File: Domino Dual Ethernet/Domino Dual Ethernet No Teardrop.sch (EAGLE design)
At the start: 38 parts, among them J1 B59(57-02)F4-03-1212-C12, J2 MH18-1, J3 MH18-1

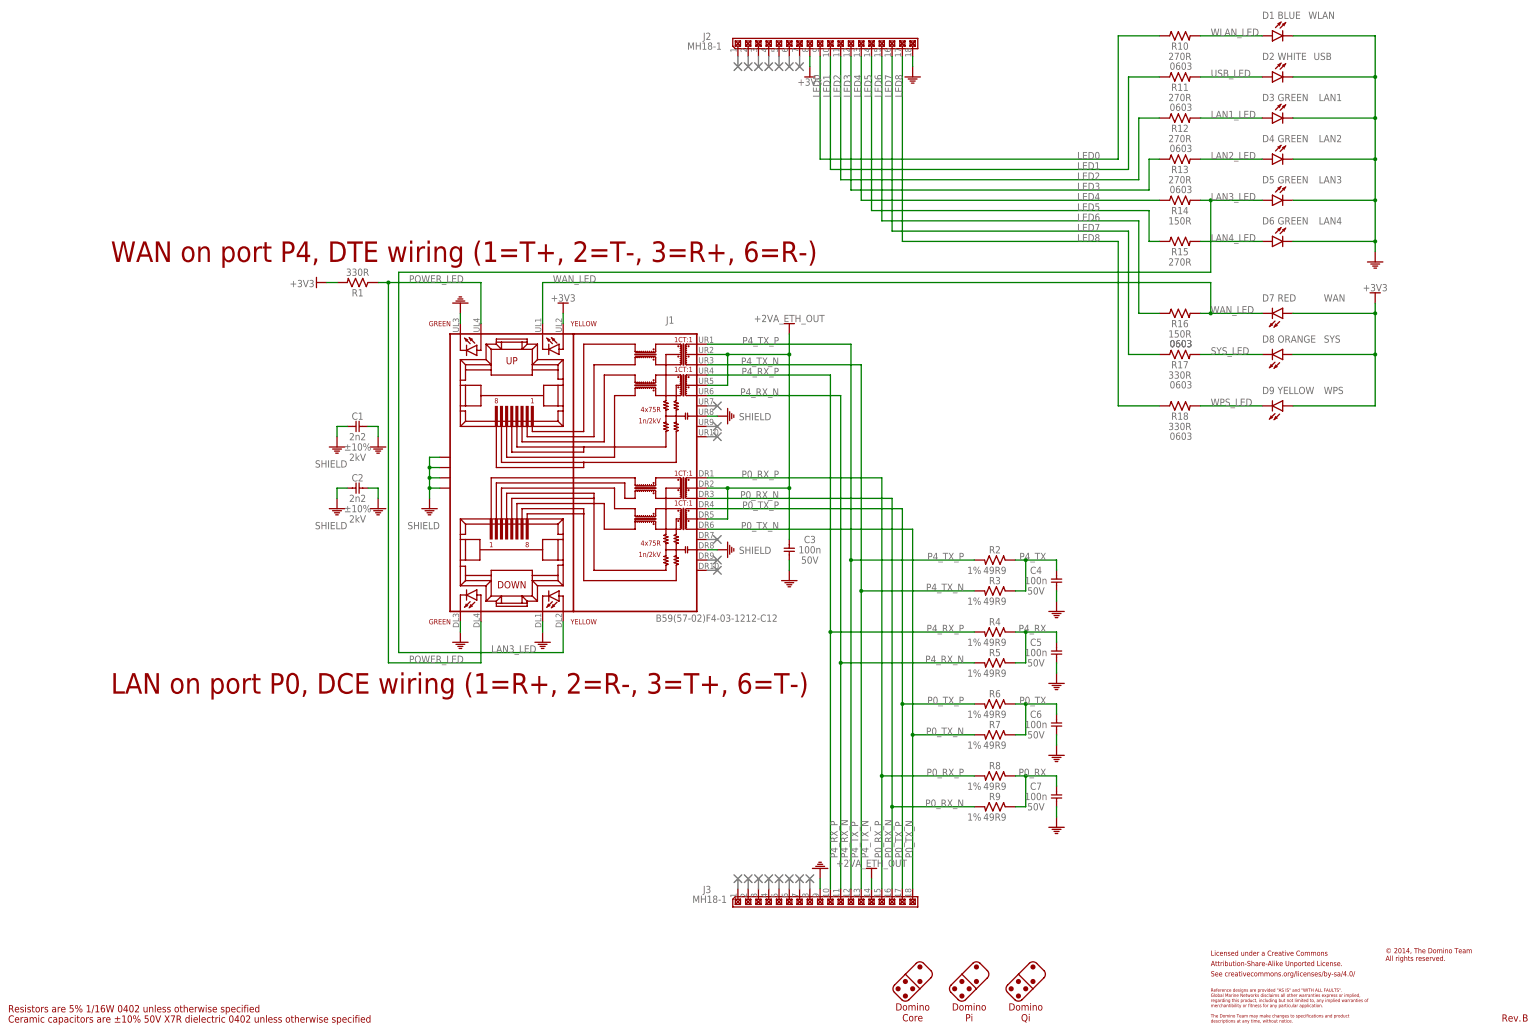
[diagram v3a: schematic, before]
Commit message: Replaced RJ45 Jack with one model without LED in Dual Ethernet tile
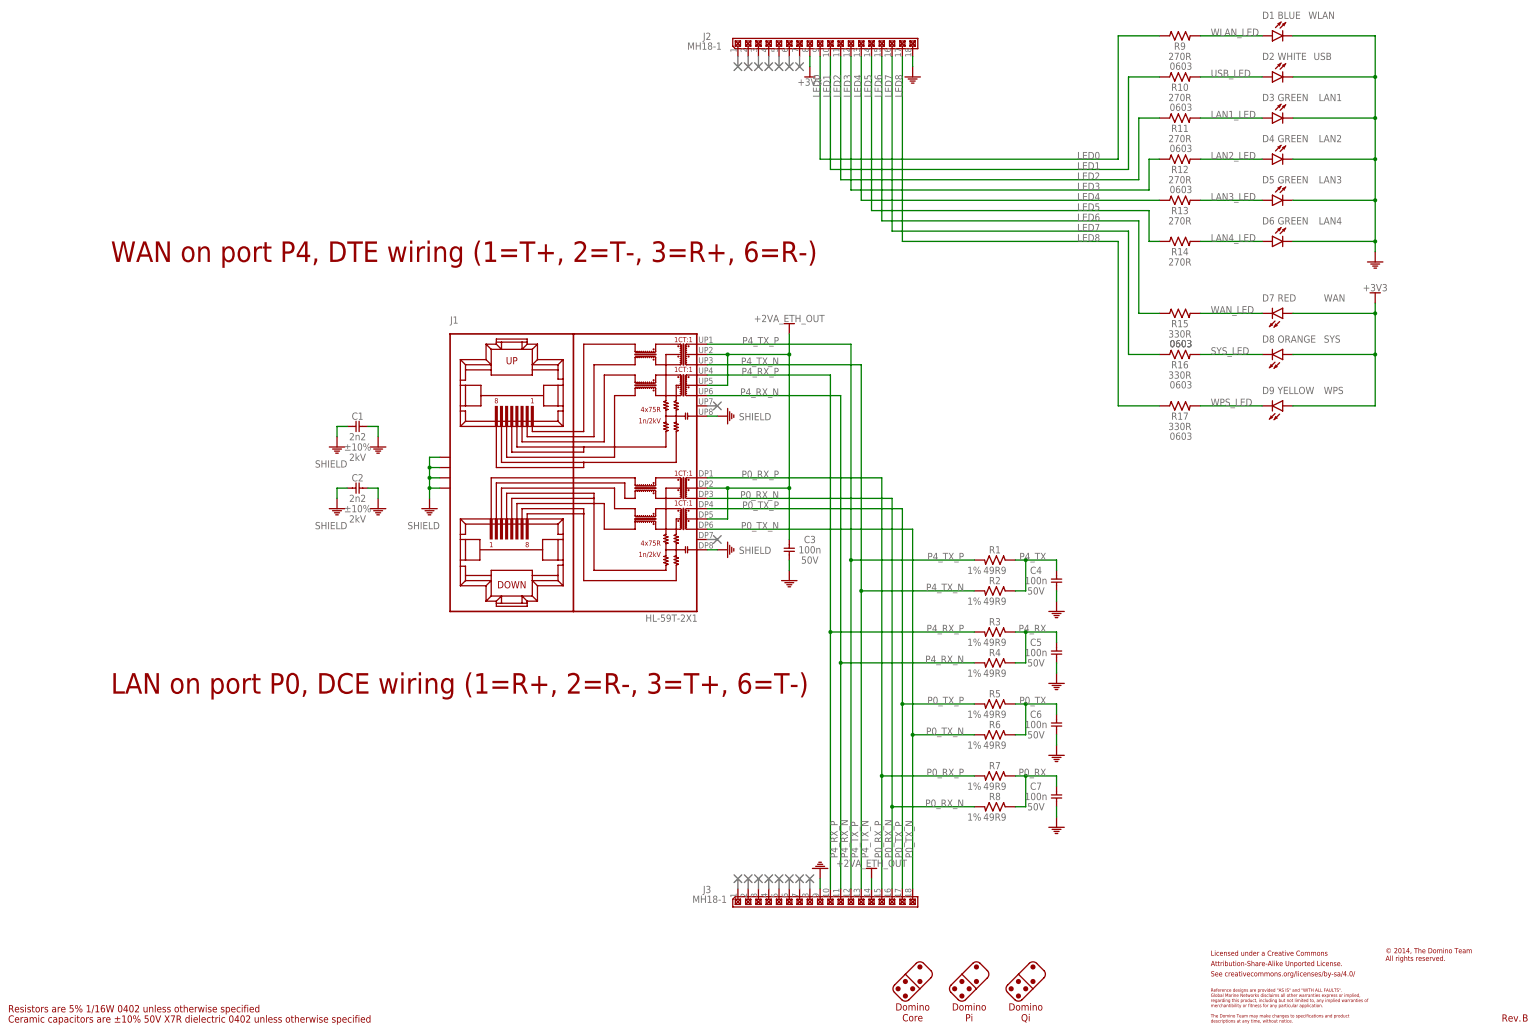
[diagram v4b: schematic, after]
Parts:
- removed R18: 330R, Domino:RES_0603
- J1: value B59(57-02)F4-03-1212-C12 -> HL-59T-2X1; device Domino:B59(57-02)F4-03-1212-C12 -> Domino:HL-59T-2X1; PARTNO B59(57-02)F4-03-1212-C12 -> HL-59T-2X1
- R1: value 330R -> 49R9; device Domino:RES_0603 -> Domino:RES_0402; PARTNO R0603_330R_5%_125mW -> R0402_49R9_1%_62.5mW; TOL 5% -> 1%
- R14: value 150R -> 270R; PARTNO R0603_150R_5%_125mW -> R0603_270R_5%_125mW
- R15: value 270R -> 330R; PARTNO R0603_270R_5%_125mW -> R0603_330R_5%_125mW
- R16: value 150R -> 330R; PARTNO R0603_150R_5%_125mW -> R0603_330R_5%_125mW
- R9: value 49R9 -> 270R; device Domino:RES_0402 -> Domino:RES_0603; PARTNO R0402_49R9_1%_62.5mW -> R0603_270R_5%_125mW; RATE 62.5mW -> 125mW; TOL 1% -> 5%
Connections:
- removed net POWER_LED: J1.DL4, J1.UL4, R1.1
- net +3V3: no longer J1.UL2, R1.2
- net GND: no longer J1.DL1, J1.DL3, J1.UL3
- net LAN1_LED: now also R11.2; no longer R12.2
- net LAN2_LED: now also R12.2; no longer R13.2
- net LAN3_LED: now also R13.2; no longer J1.DL2, R14.2
- net LAN4_LED: now also R14.2; no longer R15.2
- net LED0: now also R9.1; no longer R10.1
- net LED1: now also R10.1; no longer R11.1
- net LED2: now also R11.1; no longer R12.1
- net LED3: now also R12.1; no longer R13.1
- net LED4: now also R13.1; no longer R14.1
- net LED5: now also R14.1; no longer R15.1
- net LED6: now also R15.1; no longer R16.1
- net LED7: now also R16.1; no longer R17.1
- net LED8: now also R17.1; no longer R18.1
- net P0_RX: now also R7.1; no longer R9.1
- net P0_RX_N: now also R8.2; no longer R9.2
- net P0_RX_P: now also R7.2; no longer R8.2
- net P0_TX: now also R5.1; no longer R7.1
- net P0_TX_N: now also R6.2; no longer R7.2
- net P0_TX_P: now also R5.2; no longer R6.2
- net P4_RX: now also R3.1; no longer R5.1
- net P4_RX_N: now also R4.2; no longer R5.2
- net P4_RX_P: now also R3.2; no longer R4.2
- net P4_TX: now also R1.1; no longer R3.1
- net P4_TX_N: now also R2.2; no longer R3.2
- net P4_TX_P: now also R1.2; no longer R2.2
- net SYS_LED: now also R16.2; no longer R17.2
- net USB_LED: now also R10.2; no longer R11.2
- net WAN_LED: now also R15.2; no longer J1.UL1, R16.2
- net WLAN_LED: now also R9.2; no longer R10.2
- net WPS_LED: now also R17.2; no longer R18.2
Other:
- moved on the sheet: R1, R10, R11, R12, R13, R14, R15, R16, R17, R2, R3, R4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
